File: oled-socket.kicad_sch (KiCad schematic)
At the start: 19 parts, among them IC17 TPS6734IDR, J5 3-2328724-1

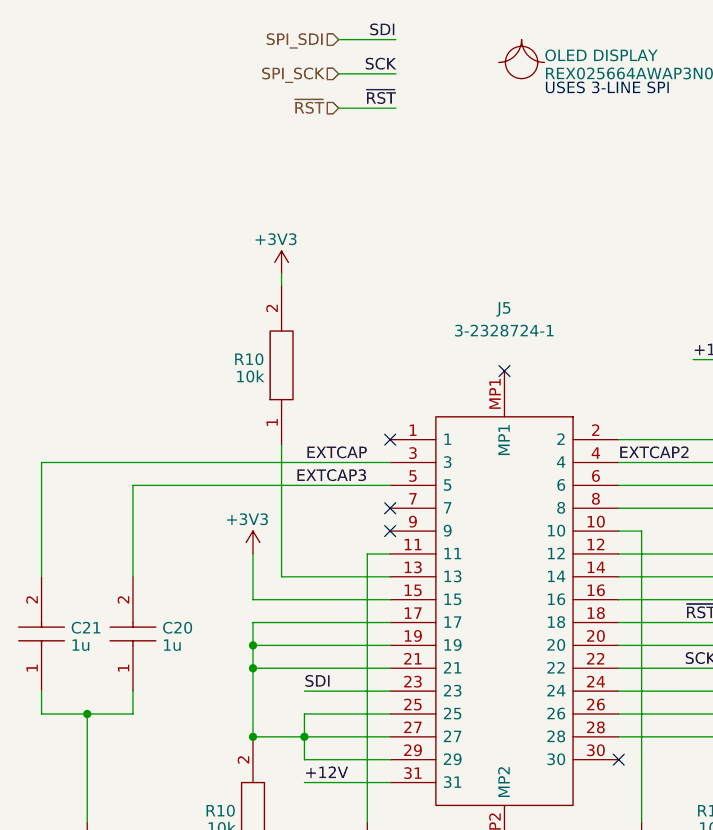
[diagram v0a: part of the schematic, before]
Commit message: switch OLED to 4-wire serial and add CS line to OLED/ethernet chips
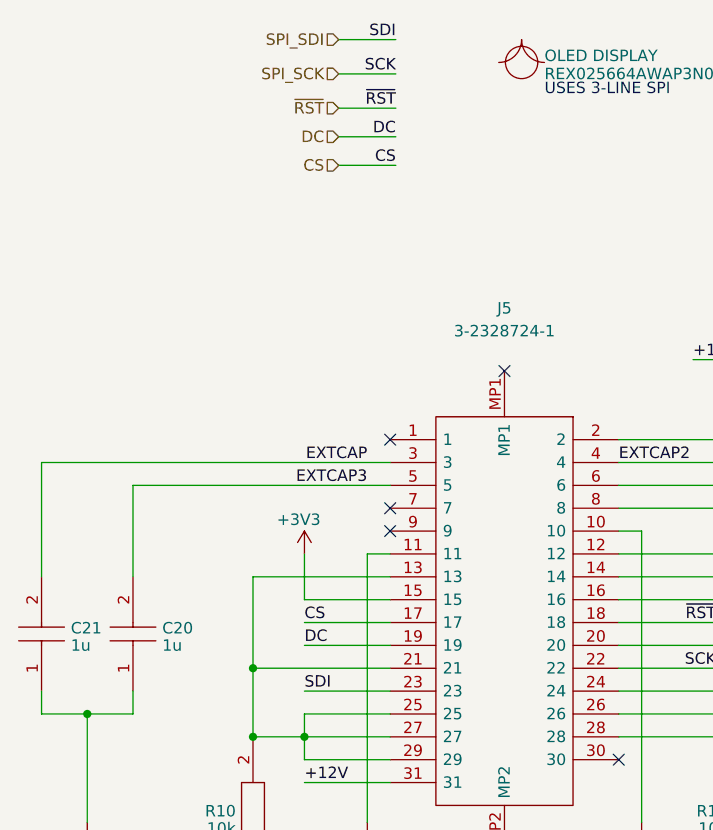
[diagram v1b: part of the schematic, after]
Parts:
- removed R10: 10k, SamacSys_Parts:RESC5025X65N, symbol SamacSys_Parts:RC2010JK-0710KL
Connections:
- net at J5.13: now also J5.21, J5.25, J5.27, J5.29, R10.2
- new net CS: J5.17
- new net DC: J5.19

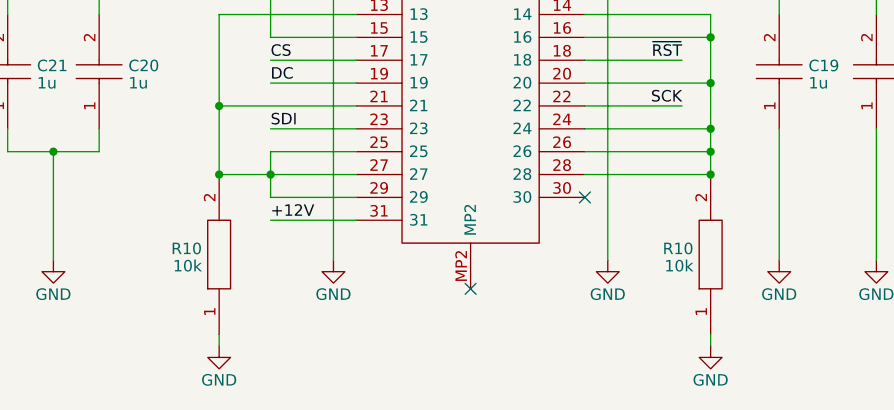
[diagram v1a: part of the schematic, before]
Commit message: remove pull-down resistor from OLED pins
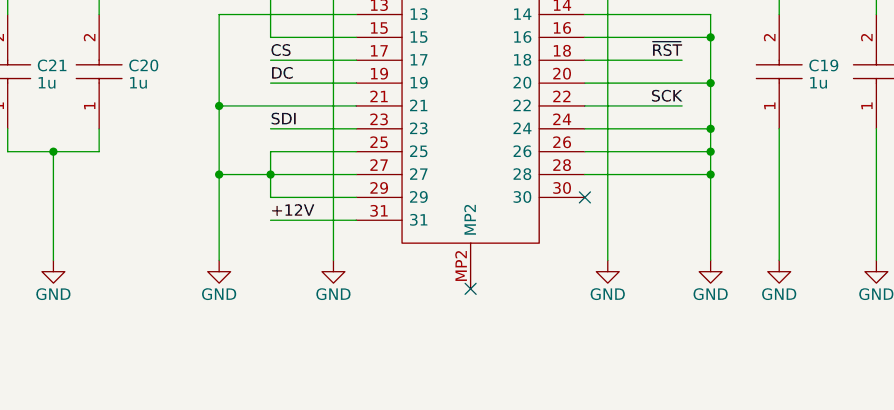
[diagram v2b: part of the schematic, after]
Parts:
- removed R10 (x2): 10k, SamacSys_Parts:RESC5025X65N, symbol SamacSys_Parts:RC2010JK-0710KL
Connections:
- net GND: now also J5.13, J5.14, J5.16, J5.20, J5.21, J5.24, J5.25, J5.26, J5.27, J5.28, J5.29
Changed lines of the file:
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@@
   (junction (at 112.395 85.09) (diameter 0) (color 0 0 0 0)
   )
+  (junction (at 58.42 118.11) (diameter 0) (color 0 0 0 0)
+  )
   (junction (at 58.42 110.49) (diameter 0) (color 0 0 0 0)
   )
@@
   (junction (at 113.03 115.57) (diameter 0) (color 0 0 0 0)
   )
+  (junction (at 113.03 118.11) (diameter 0) (color 0 0 0 0)
+  )
   (junction (at 112.395 80.01) (diameter 0) (color 0 0 0 0)
   )
   (junction (at 113.03 113.03) (diameter 0) (color 0 0 0 0)
   )
-  (junction (at 113.03 118.11) (diameter 0) (color 0 0 0 0)
-  )
   (junction (at 113.03 107.95) (diameter 0) (color 0 0 0 0)
-  )
-  (junction (at 58.42 118.11) (diameter 0) (color 0 0 0 0)
   )
   (junction (at 236.22 119.38) (diameter 0) (color 0 0 0 0)
@@
     (stroke (width 0) (type default))
   )
+  (wire (pts (xy 113.03 118.11) (xy 113.03 127.635))
+    (stroke (width 0) (type default))
+  )
   (wire (pts (xy 107.315 76.2) (xy 112.395 76.2))
     (stroke (width 0) (type default))
@@
     (stroke (width 0) (type dot))
   )
-  (wire (pts (xy 113.03 135.89) (xy 113.03 137.16))
-    (stroke (width 0) (type default))
-  )
   (wire (pts (xy 223.52 87.63) (xy 220.98 87.63))
     (stroke (width 0) (type default))
@@
     (stroke (width 0) (type default))
   )
+  (wire (pts (xy 58.42 118.11) (xy 58.42 127.635))
+    (stroke (width 0) (type default))
+  )
   (wire (pts (xy 73.66 97.79) (xy 71.12 97.79))
     (stroke (width 0) (type default))
@@
   )
   (wire (pts (xy 40.005 115.57) (xy 45.085 115.57))
-    (stroke (width 0) (type default))
-  )
-  (wire (pts (xy 58.42 137.16) (xy 58.42 135.89))
     (stroke (width 0) (type default))
   )
@@
         (path "/e89dcd22-1250-4a5b-b778-1c95a0dd623d/1b3eede1-74b0-4c0b-b4f1-7ec1bfc1f54f"
           (reference "C27") (unit 1)
-        )
-      )
-    )
-  )
-  (symbol (lib_id "SamacSys_Parts:RC2010JK-0710KL") (at 113.03 135.89 90) (unit 1)
-    (in_bom yes) (on_board yes) (dnp no)
-    (property "Reference" "R10" (at 111.125 126.365 90)
-      (effects (font (size 1.27 1.27)) (justify left))
-    )
-    (property "Value" "10k" (at 111.125 128.286 90)
-      (effects (font (size 1.27 1.27)) (justify left))
-    )
-    (property "Footprint" "SamacSys_Parts:RESC5025X65N" (at 111.76 121.92 0)
-      (effects (font (size 1.27 1.27)) (justify left) hide)
-    )
-    (property "Datasheet" "https://www.arrow.com/en/products/rc2010jk-0710kl/yageo" (at 114.3 121.92 0)
-      (effects (font (size 1.27 1.27)) (justify left) hide)
-    )
-    (property "Description" "Res Thick Film 2010 10K Ohm 5% 0.75W(3/4W) +/-100ppm/C Pad SMD T/R" (at 116.84 121.92 0)
-      (effects (font (size 1.27 1.27)) (justify left) hide)
-    )
-    (property "Height" "0.65" (at 119.38 121.92 0)
-      (effects (font (size 1.27 1.27)) (justify left) hide)
-    )
-    (property "Manufacturer_Name" "KEMET" (at 121.92 121.92 0)
-      (effects (font (size 1.27 1.27)) (justify left) hide)
-    )
-    (property "Manufacturer_Part_Number" "RC2010JK-0710KL" (at 124.46 121.92 0)
-      (effects (font (size 1.27 1.27)) (justify left) hide)
-    )
-    (property "Mouser Part Number" "603-RC2010JK-0710KL" (at 127 121.92 0)
-      (effects (font (size 1.27 1.27)) (justify left) hide)
-    )
-    (property "Mouser Price/Stock" "https://www.mouser.co.uk/ProductDetail/YAGEO/RC2010JK-0710KL?qs=sNpmnPgvziOLj5uuquGIow%3D%3D" (at 129.54 121.92 0)
-      (effects (font (size 1.27 1.27)) (justify left) hide)
-    )
-    (property "Arrow Part Number" "RC2010JK-0710KL" (at 132.08 121.92 0)
-      (effects (font (size 1.27 1.27)) (justify left) hide)
-    )
-    (property "Arrow Price/Stock" "https://www.arrow.com/en/products/rc2010jk-0710kl/yageo" (at 134.62 121.92 0)
-      (effects (font (size 1.27 1.27)) (justify left) hide)
-    )
-    (property "Mouser Testing Part Number" "" (at 137.16 121.92 0)
-      (effects (font (size 1.27 1.27)) (justify left) hide)
-    )
-    (property "Mouser Testing Price/Stock" "" (at 139.7 121.92 0)
-      (effects (font (size 1.27 1.27)) (justify left) hide)
-    )
-    (pin "1")
-    (pin "2")
-    (instances
-      (project "Oro Testbed v2"
-        (path "/3d0fc623-63eb-45e5-a304-e470d9b3a173"
-          (reference "R10") (unit 1)
-        )
-        (path "/3d0fc623-63eb-45e5-a304-e470d9b3a173/7310340d-2c15-4c32-b17d-f4923dae9f8e"
-          (reference "R8") (unit 1)
-        )
-      )
-      (project "OroLink"
-        (path "/e89dcd22-1250-4a5b-b778-1c95a0dd623d/1b3eede1-74b0-4c0b-b4f1-7ec1bfc1f54f"
-          (reference "R10") (unit 1)
         )
       )
@@
     )
   )
-  (symbol (lib_id "power:GND") (at 58.42 137.16 0) (unit 1)
+  (symbol (lib_id "power:GND") (at 58.42 127.635 0) (mirror y) (unit 1)
     (in_bom yes) (on_board yes) (dnp no)
-    (property "Reference" "#PWR018" (at 58.42 143.51 0)
-      (effects (font (size 1.27 1.27)) hide)
-    )
-    (property "Value" "GND" (at 58.42 140.97 0)
-      (effects (font (size 1.27 1.27)))
-    )
-    (property "Footprint" "" (at 58.42 137.16 0)
-      (effects (font (size 1.27 1.27)) hide)
-    )
-    (property "Datasheet" "" (at 58.42 137.16 0)
+    (property "Reference" "#PWR018" (at 58.42 133.985 0)
+      (effects (font (size 1.27 1.27)) hide)
+    )
+    (property "Value" "GND" (at 58.42 131.445 0)
+      (effects (font (size 1.27 1.27)))
+    )
+    (property "Footprint" "" (at 58.42 127.635 0)
+      (effects (font (size 1.27 1.27)) hide)
+    )
+    (property "Datasheet" "" (at 58.42 127.635 0)
       (effects (font (size 1.27 1.27)) hide)
     )
@@
         (path "/e89dcd22-1250-4a5b-b778-1c95a0dd623d/1b3eede1-74b0-4c0b-b4f1-7ec1bfc1f54f"
           (reference "#PWR029") (unit 1)
-        )
-      )
-    )
-  )
-  (symbol (lib_id "SamacSys_Parts:RC2010JK-0710KL") (at 58.42 135.89 90) (unit 1)
-    (in_bom yes) (on_board yes) (dnp no)
-    (property "Reference" "R10" (at 56.515 126.365 90)
-      (effects (font (size 1.27 1.27)) (justify left))
-    )
-    (property "Value" "10k" (at 56.515 128.286 90)
-      (effects (font (size 1.27 1.27)) (justify left))
-    )
-    (property "Footprint" "SamacSys_Parts:RESC5025X65N" (at 57.15 121.92 0)
-      (effects (font (size 1.27 1.27)) (justify left) hide)
-    )
-    (property "Datasheet" "https://www.arrow.com/en/products/rc2010jk-0710kl/yageo" (at 59.69 121.92 0)
-      (effects (font (size 1.27 1.27)) (justify left) hide)
-    )
-    (property "Description" "Res Thick Film 2010 10K Ohm 5% 0.75W(3/4W) +/-100ppm/C Pad SMD T/R" (at 62.23 121.92 0)
-      (effects (font (size 1.27 1.27)) (justify left) hide)
-    )
-    (property "Height" "0.65" (at 64.77 121.92 0)
-      (effects (font (size 1.27 1.27)) (justify left) hide)
-    )
-    (property "Manufacturer_Name" "KEMET" (at 67.31 121.92 0)
-      (effects (font (size 1.27 1.27)) (justify left) hide)
-    )
-    (property "Manufacturer_Part_Number" "RC2010JK-0710KL" (at 69.85 121.92 0)
-      (effects (font (size 1.27 1.27)) (justify left) hide)
-    )
-    (property "Mouser Part Number" "603-RC2010JK-0710KL" (at 72.39 121.92 0)
-      (effects (font (size 1.27 1.27)) (justify left) hide)
-    )
-    (property "Mouser Price/Stock" "https://www.mouser.co.uk/ProductDetail/YAGEO/RC2010JK-0710KL?qs=sNpmnPgvziOLj5uuquGIow%3D%3D" (at 74.93 121.92 0)
-      (effects (font (size 1.27 1.27)) (justify left) hide)
-    )
-    (property "Arrow Part Number" "RC2010JK-0710KL" (at 77.47 121.92 0)
-      (effects (font (size 1.27 1.27)) (justify left) hide)
-    )
-    (property "Arrow Price/Stock" "https://www.arrow.com/en/products/rc2010jk-0710kl/yageo" (at 80.01 121.92 0)
-      (effects (font (size 1.27 1.27)) (justify left) hide)
-    )
-    (property "Mouser Testing Part Number" "" (at 82.55 121.92 0)
-      (effects (font (size 1.27 1.27)) (justify left) hide)
-    )
-    (property "Mouser Testing Price/Stock" "" (at 85.09 121.92 0)
-      (effects (font (size 1.27 1.27)) (justify left) hide)
-    )
-    (pin "1")
-    (pin "2")
-    (instances
-      (project "Oro Testbed v2"
-        (path "/3d0fc623-63eb-45e5-a304-e470d9b3a173"
-          (reference "R10") (unit 1)
-        )
-        (path "/3d0fc623-63eb-45e5-a304-e470d9b3a173/7310340d-2c15-4c32-b17d-f4923dae9f8e"
-          (reference "R8") (unit 1)
-        )
-      )
-      (project "OroLink"
-        (path "/e89dcd22-1250-4a5b-b778-1c95a0dd623d/1b3eede1-74b0-4c0b-b4f1-7ec1bfc1f54f"
-          (reference "R8") (unit 1)
         )
       )
@@
     )
   )
-  (symbol (lib_id "power:GND") (at 113.03 137.16 0) (mirror y) (unit 1)
+  (symbol (lib_id "power:GND") (at 113.03 127.635 0) (mirror y) (unit 1)
     (in_bom yes) (on_board yes) (dnp no)
-    (property "Reference" "#PWR026" (at 113.03 143.51 0)
-      (effects (font (size 1.27 1.27)) hide)
-    )
-    (property "Value" "GND" (at 113.03 140.97 0)
-      (effects (font (size 1.27 1.27)))
-    )
-    (property "Footprint" "" (at 113.03 137.16 0)
-      (effects (font (size 1.27 1.27)) hide)
-    )
-    (property "Datasheet" "" (at 113.03 137.16 0)
-      (effects (font (size 1.27 1.27)) hide)
-    )
+    (property "Reference" "#PWR026" (at 113.03 133.985 0)
+      (effects (font (size 1.27 1.27)) hide)
+    )
+    (property "Value" "GND" (at 113.03 131.445 0)
+      (effects (font (size 1.27 1.27)))
+    )
+    (property "Footprint" "" (at 113.03 127.635 0)
+      (effects (font (size 1.27 1.27)) hide)
+    )
+    (property "Datasheet" "" (at 113.03 127.635 0)
+      (effects (font (size 1.27 1.27)) hide)
+    )

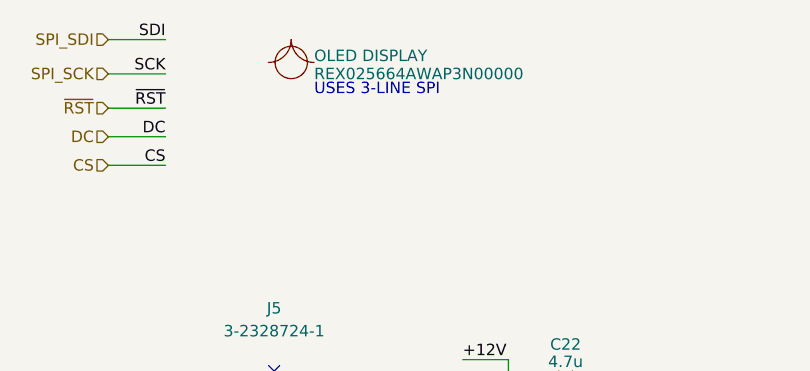
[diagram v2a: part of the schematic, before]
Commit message: fix OLED note: 3-LINE SPI -> 4-WIRE SPI
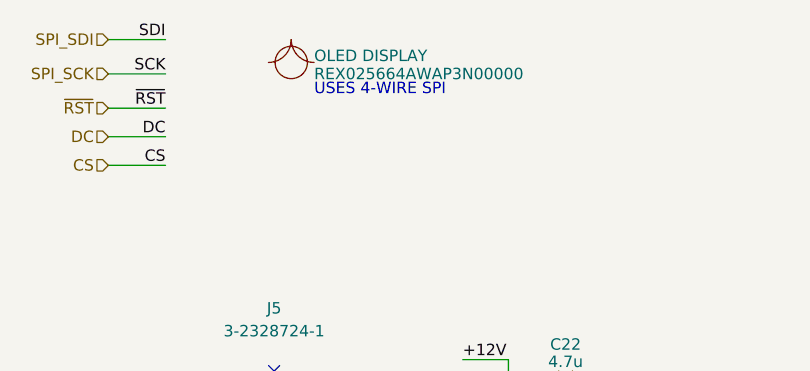
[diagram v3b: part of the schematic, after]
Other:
- note added: "USES 4-WIRE SPI"
- note removed: "USES 3-LINE SPI"
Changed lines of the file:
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@@
     (stroke (width 0) (type default))
   )
-  (text "USES 3-LINE SPI" (at 90.805 46.99 0)
+  (text "USES 4-WIRE SPI" (at 90.805 46.99 0)
     (effects (font (size 1.27 1.27)) (justify left bottom))
   )

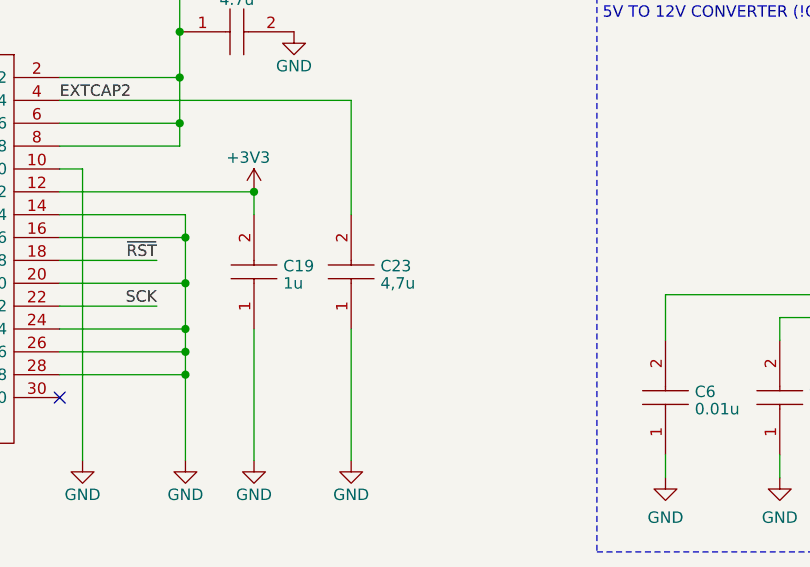
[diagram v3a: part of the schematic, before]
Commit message: fix resistor part numbers for ethernet lines
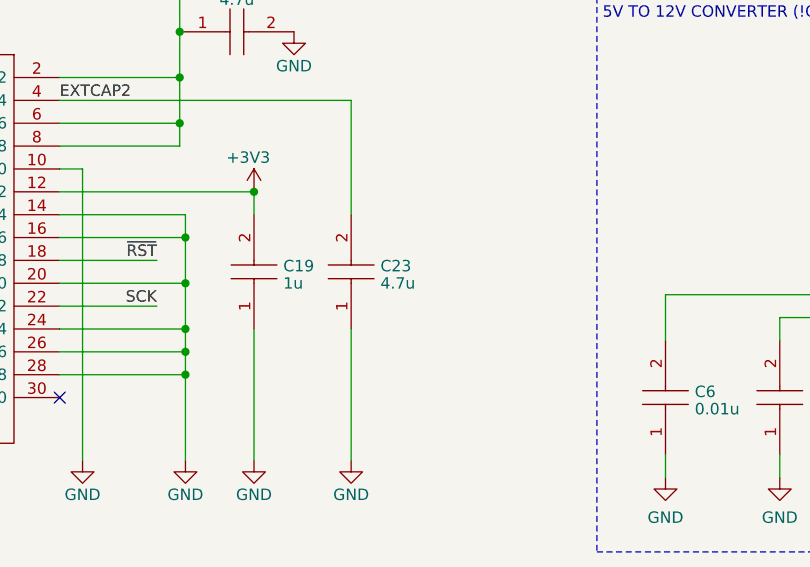
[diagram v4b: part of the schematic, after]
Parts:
- C23: value 4,7u -> 4.7u
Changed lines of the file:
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@@
       (effects (font (size 1.27 1.27)) (justify right))
     )
-    (property "Value" "4,7u" (at 134.6962 107.9573 90)
+    (property "Value" "4.7u" (at 134.6962 107.9573 90)
       (effects (font (size 1.27 1.27)) (justify right))
     )
